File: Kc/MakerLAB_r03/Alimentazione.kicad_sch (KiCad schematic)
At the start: 25 parts, among them J4 Barrel_Jack_MountingPin, J5 Conn_01x03, J6 Conn_01x03, J7 Conn_01x03, J8 Conn_01x03, SW1 SwGenerale, U1 LM317_TO-220, U2 LM7805_TO220

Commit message: 20230309-Update
Lavoro in tandem con Marco
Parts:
- removed C3: C_Polarized, symbol Device:C_Polarized
- removed J5: Conn_01x03, Connector_PinHeader_2.54mm:PinHeader_1x03_P2.54mm_Vertical, symbol Connector_Generic:Conn_01x03
- added C16, C23, C24, C3: 100nF, Capacitor_THT:C_Disc_D7.0mm_W2.5mm_P5.00mm, symbol Device:C
- added C25: 220uF, Capacitor_THT:CP_Radial_D10.0mm_P5.00mm, symbol Device:C_Polarized
- added D20: 1N400x, symbol Device:D
- added D21, D22: LED, symbol Device:LED
- added J28, J31, J32: Conn_01x03, Connector_PinHeader_2.54mm:PinHeader_1x03_P2.54mm_Vertical, symbol Connector_Generic:Conn_01x03
- added J29, J30, J5: Conn_01x02_Male, Connector_PinSocket_2.54mm:PinSocket_1x02_P2.54mm_Vertical, symbol Connector:Conn_01x02_Male
- added Q5: 2N3904, Package_TO_SOT_THT:TO-92_Inline, symbol Transistor_BJT:2N3904
- added R22, R23, R24: R, symbol Device:R
- added TP14: VarA+, TestPoint:TestPoint_Loop_D3.80mm_Drill2.8mm, symbol Connector:TestPoint
- added TP15: VarA-, TestPoint:TestPoint_Loop_D3.80mm_Drill2.8mm, symbol Connector:TestPoint
- added TP16: 5VA+, TestPoint:TestPoint_Loop_D3.80mm_Drill2.8mm, symbol Connector:TestPoint
- added TP17: 3.3VA+, TestPoint:TestPoint_Loop_D3.80mm_Drill2.8mm, symbol Connector:TestPoint
- added TP18: 5VA-, TestPoint:TestPoint_Loop_D3.80mm_Drill2.8mm, symbol Connector:TestPoint
- added TP19: 3.3VA-, TestPoint:TestPoint_Loop_D3.80mm_Drill2.8mm, symbol Connector:TestPoint
- added U11: L78L33_SOT89, Package_TO_SOT_SMD:SOT-223, symbol Regulator_Linear:L78L33_SOT89
- C1: footprint Capacitor_THT:CP_Axial_L37.0mm_D13.0mm_P43.00mm_Horizontal -> Capacitor_THT:CP_Radial_D17.0mm_P7.50mm
- C2, C5: footprint Capacitor_THT:C_Axial_L5.1mm_D3.1mm_P7.50mm_Horizontal -> Capacitor_THT:C_Disc_D7.0mm_W2.5mm_P5.00mm
- C4: value C_Polarized -> 10uF; footprint (none) -> Capacitor_THT:CP_Radial_D5.0mm_P2.00mm
- C6: value 10uF -> 220uF; footprint Capacitor_THT:CP_Axial_L37.0mm_D13.0mm_P43.00mm_Horizontal -> Capacitor_THT:CP_Radial_D10.0mm_P5.00mm
- C7: value C_Polarized -> 220uF; footprint (none) -> Capacitor_THT:CP_Radial_D10.0mm_P5.00mm
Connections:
- net +5V: now also D21.2 (A), D22.2 (A), J29.2 (Pin_2), J30.2 (Pin_2), J31.1 (Pin_1), J31.2 (Pin_2), J31.3 (Pin_3), TP18.1, TP19.1; no longer C5.1, C6.1, D4.2 (A), U2.3 (VO)
- net +Vvar: now also J7.1 (Pin_1), J7.2 (Pin_2), J7.3 (Pin_3), C23.1, J5.2 (Pin_2), R22.2, TP15.1; no longer C7.1, D3.2 (A), D5.1 (K), R2.1, RV1.1, U1.2 (VO)
- net GND: now also C16.2, C23.2, C24.2, C25.2, C3.2, J28.1 (Pin_1), J28.2 (Pin_2), J28.3 (Pin_3), J32.1 (Pin_1), J32.2 (Pin_2), J32.3 (Pin_3), Q5.1 (E), R23.2, R24.2, U11.2 (GND); no longer J7.1 (Pin_1), J7.2 (Pin_2), J7.3 (Pin_3), R1.2
- net at C1.1, C2.1, D2.2 (A)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: now also C3.1
- new net: C7.1, D3.2 (A), D5.1 (K), J5.1 (Pin_1), R2.1, RV1.1, TP14.1, U1.2 (VO)
- new net: D21.1 (K), R23.1
- new net: C16.1, C5.1, C6.1, D20.1 (K), D4.2 (A), J29.1 (Pin_1), TP16.1, U11.3 (IN), U2.3 (VO)
- new net: C24.1, C25.1, D20.2 (A), J30.1 (Pin_1), TP17.1, U11.1 (OUT)
- new net: Q5.3 (C), R1.2
- new net: Q5.2 (B), R22.1
- new net: D22.1 (K), R24.1
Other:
- moved on the sheet: C1, D1, J4, L1, SW1

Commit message: Power Unit
Iniziato a sistemare l'unità alimentatore
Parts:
- D2: value LED -> VarOut; footprint (none) -> LED_THT:LED_D5.0mm
- D21: value LED -> +5V; footprint (none) -> LED_THT:LED_D5.0mm
- D22: value LED -> +3.3V; footprint (none) -> LED_THT:LED_D5.0mm
- R1, R2, R22, R23, R24: footprint (none) -> Resistor_THT:R_Axial_DIN0207_L6.3mm_D2.5mm_P10.16mm_Horizontal
- SW1: footprint Connector_PinSocket_2.54mm:PinSocket_1x03_P2.54mm_Vertical -> Button_Switch_THT:SW_100SP1T2B4M7QE
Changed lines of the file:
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@@
       (effects (font (size 1.27 1.27)) (justify left))
     )
-    (property "Footprint" "" (id 2) (at 220.472 50.8 90)
+    (property "Footprint" "Resistor_THT:R_Axial_DIN0207_L6.3mm_D2.5mm_P10.16mm_Horizontal" (id 2) (at 220.472 50.8 90)
       (effects (font (size 1.27 1.27)) hide)
     )
@@
       (effects (font (size 1.27 1.27)) (justify left))
     )
-    (property "Footprint" "" (id 2) (at 33.782 157.48 90)
+    (property "Footprint" "Resistor_THT:R_Axial_DIN0207_L6.3mm_D2.5mm_P10.16mm_Horizontal" (id 2) (at 33.782 157.48 90)
       (effects (font (size 1.27 1.27)) hide)
     )
@@
       (effects (font (size 1.27 1.27)) (justify left))
     )
-    (property "Footprint" "Connector_PinSocket_2.54mm:PinSocket_1x03_P2.54mm_Vertical" (id 2) (at 55.88 90.17 0)
+    (property "Footprint" "Button_Switch_THT:SW_100SP1T2B4M7QE" (id 2) (at 55.88 90.17 0)
       (effects (font (size 1.27 1.27)) hide)
     )
@@
       (effects (font (size 1.27 1.27)) (justify right))
     )
-    (property "Value" "LED" (id 1) (at 227.33 106.9974 90)
-      (effects (font (size 1.27 1.27)) (justify right))
-    )
-    (property "Footprint" "" (id 2) (at 223.52 104.14 0)
+    (property "Value" "+3.3V" (id 1) (at 227.33 106.9974 90)
+      (effects (font (size 1.27 1.27)) (justify right))
+    )
+    (property "Footprint" "LED_THT:LED_D5.0mm" (id 2) (at 223.52 104.14 0)
       (effects (font (size 1.27 1.27)) hide)
     )
@@
       (effects (font (size 1.27 1.27)) (justify left))
     )
-    (property "Footprint" "" (id 2) (at 76.962 158.75 90)
+    (property "Footprint" "Resistor_THT:R_Axial_DIN0207_L6.3mm_D2.5mm_P10.16mm_Horizontal" (id 2) (at 76.962 158.75 90)
       (effects (font (size 1.27 1.27)) hide)
     )
@@
       (effects (font (size 1.27 1.27)) (justify right))
     )
-    (property "Value" "LED" (id 1) (at 226.06 46.0374 90)
-      (effects (font (size 1.27 1.27)) (justify right))
-    )
-    (property "Footprint" "" (id 2) (at 222.25 43.18 0)
+    (property "Value" "+5V" (id 1) (at 226.06 46.0374 90)
+      (effects (font (size 1.27 1.27)) (justify right))
+    )
+    (property "Footprint" "LED_THT:LED_D5.0mm" (id 2) (at 222.25 43.18 0)
       (effects (font (size 1.27 1.27)) hide)
     )
@@
       (effects (font (size 1.27 1.27)) (justify right))
     )
-    (property "Value" "LED" (id 1) (at 39.37 152.7174 90)
-      (effects (font (size 1.27 1.27)) (justify right))
-    )
-    (property "Footprint" "" (id 2) (at 35.56 149.86 0)
+    (property "Value" "VarOut" (id 1) (at 39.37 152.7174 90)
+      (effects (font (size 1.27 1.27)) (justify right))
+    )
+    (property "Footprint" "LED_THT:LED_D5.0mm" (id 2) (at 35.56 149.86 0)
       (effects (font (size 1.27 1.27)) hide)
     )
@@
       (effects (font (size 1.27 1.27)) (justify left))
     )
-    (property "Footprint" "" (id 2) (at 221.742 111.76 90)
+    (property "Footprint" "Resistor_THT:R_Axial_DIN0207_L6.3mm_D2.5mm_P10.16mm_Horizontal" (id 2) (at 221.742 111.76 90)
       (effects (font (size 1.27 1.27)) hide)
     )
@@
       (effects (font (size 1.27 1.27)) (justify left))
     )
-    (property "Footprint" "" (id 2) (at 117.602 142.24 90)
-      (effects (font (size 1.27 1.27)) hide)
-    )
+    (property "Footprint" "Resistor_THT:R_Axial_DIN0207_L6.3mm_D2.5mm_P10.16mm_Horizontal" (id 2) (at 117.602 142.24 90)
+      (effects (font (size 1.27 1.27)) hide)
+    )

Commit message: Power Supply
Seconda fase
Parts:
- removed RV1: R_Potentiometer, symbol Device:R_Potentiometer
- added HS1, HS2: Heatsink, Heatsink2:Heatsink_28x25_Horiz, symbol Mechanical:Heatsink
- added Vmet1: 3,5_Digit_Voltmeter_3Wire, VoltmeterModule:3,5 Digit 0,28'' Voltmeter, symbol DigitalInstruments:3,5_Digit_Voltmeter_3Wire
- D1: value Ponte 1,5A -> D_Bridge_+AA-; footprint Diode_THT:Diode_Bridge_Round_D8.9mm -> Diode_THT:Diode_Bridge_Vishay_KBL; symbol Device:D_Bridge_+-AA -> Device:D_Bridge_+AA-
- D20, D4: footprint (none) -> Diode_THT:D_A-405_P10.16mm_Horizontal
- D3, D5: value D -> 1n4001; footprint (none) -> Diode_THT:D_A-405_P10.16mm_Horizontal
- Q5: value 2N3904 -> BC237; symbol Transistor_BJT:2N3904 -> Transistor_BJT:BC237
- R1: value R -> 3,3k
- R2: value R -> 240
- R22: value R -> 330k
- RV2: value R_Potentiometer -> 5K; footprint (none) -> Potentiometer_THT:Potentiometer_Omeg_PC16BU_Vertical
- U1, U2: footprint Package_TO_SOT_THT:TO-220-3_Vertical -> Package_TO_SOT_THT:TO-220-3_Horizontal_TabDown
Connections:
- net +Vvar: now also Vmet1.2 (Vin)
- net GND: now also D1.4 (-), Q5.3 (E), Vmet1.1 (GND); no longer D1.2 (-), Q5.1 (E)
- net at J4.1: now also D1.2; no longer D1.3
- net at J4.2: now also SW1.2 (B); no longer SW1.3 (C)
- net at C16.1, C5.1, C6.1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: now also Vmet1.3 (V+)
- net at R1.2: now also Q5.1 (C); no longer Q5.3 (C)
- new net: D1.3, SW1.3 (C)
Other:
- moved on the sheet: C7, D5, RV2, SW1

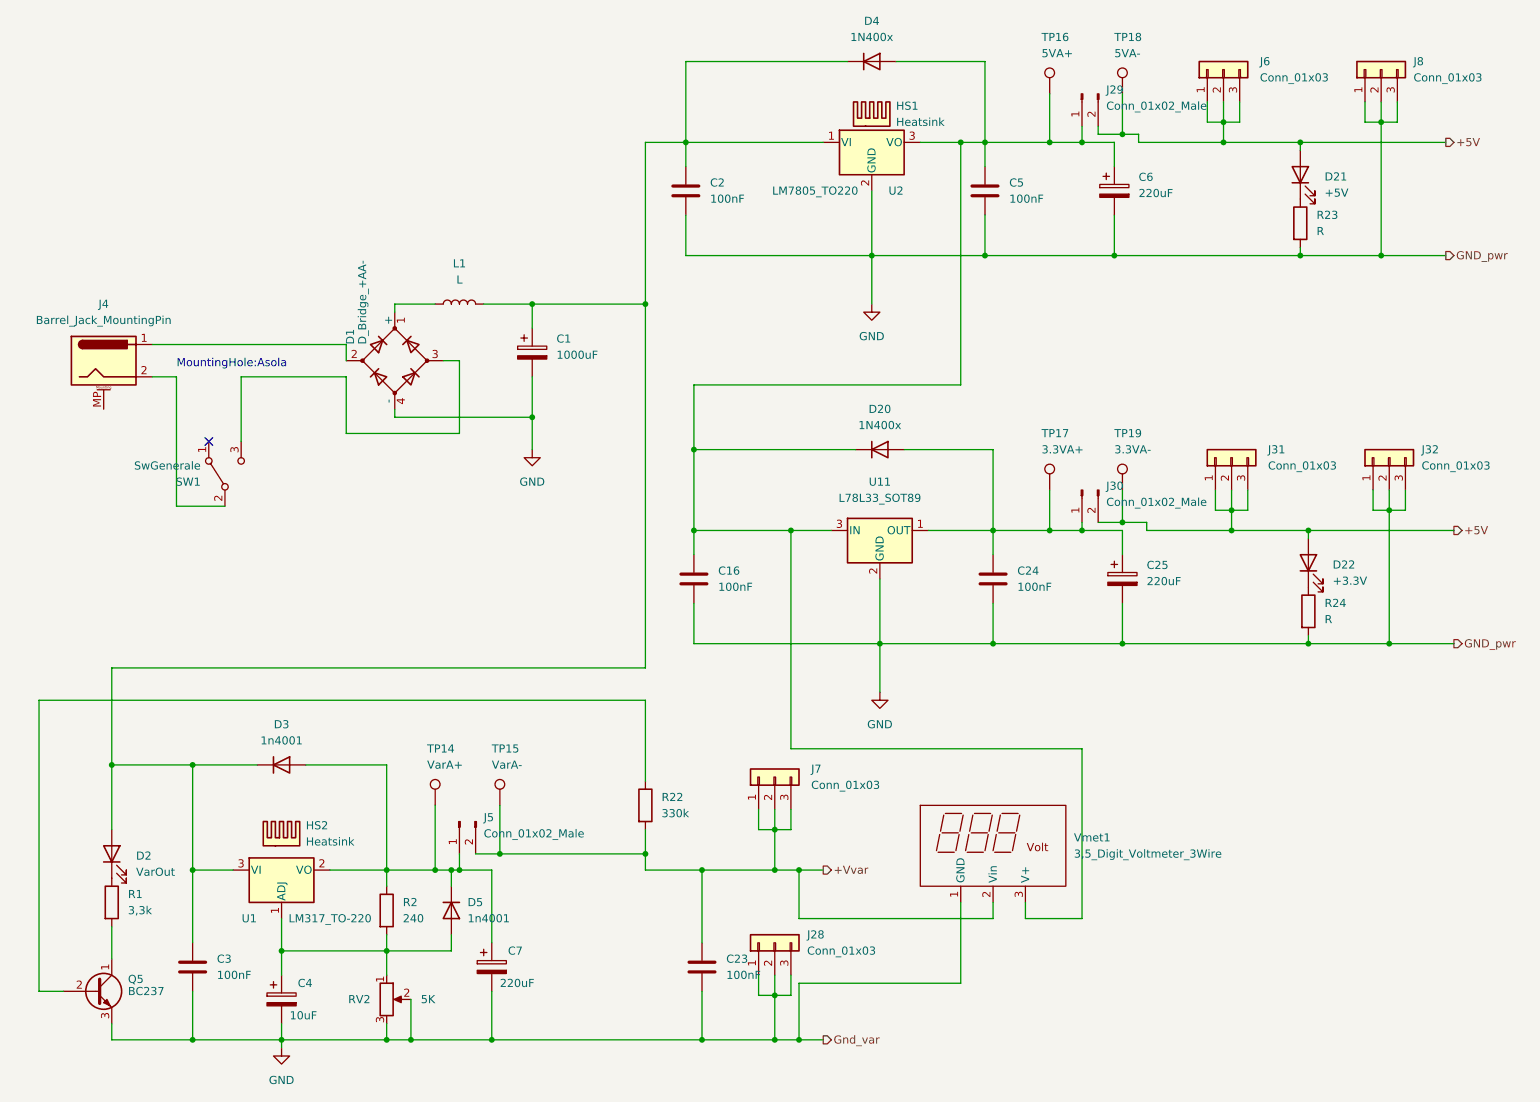
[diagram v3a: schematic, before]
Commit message: Layout Alimentatori OK
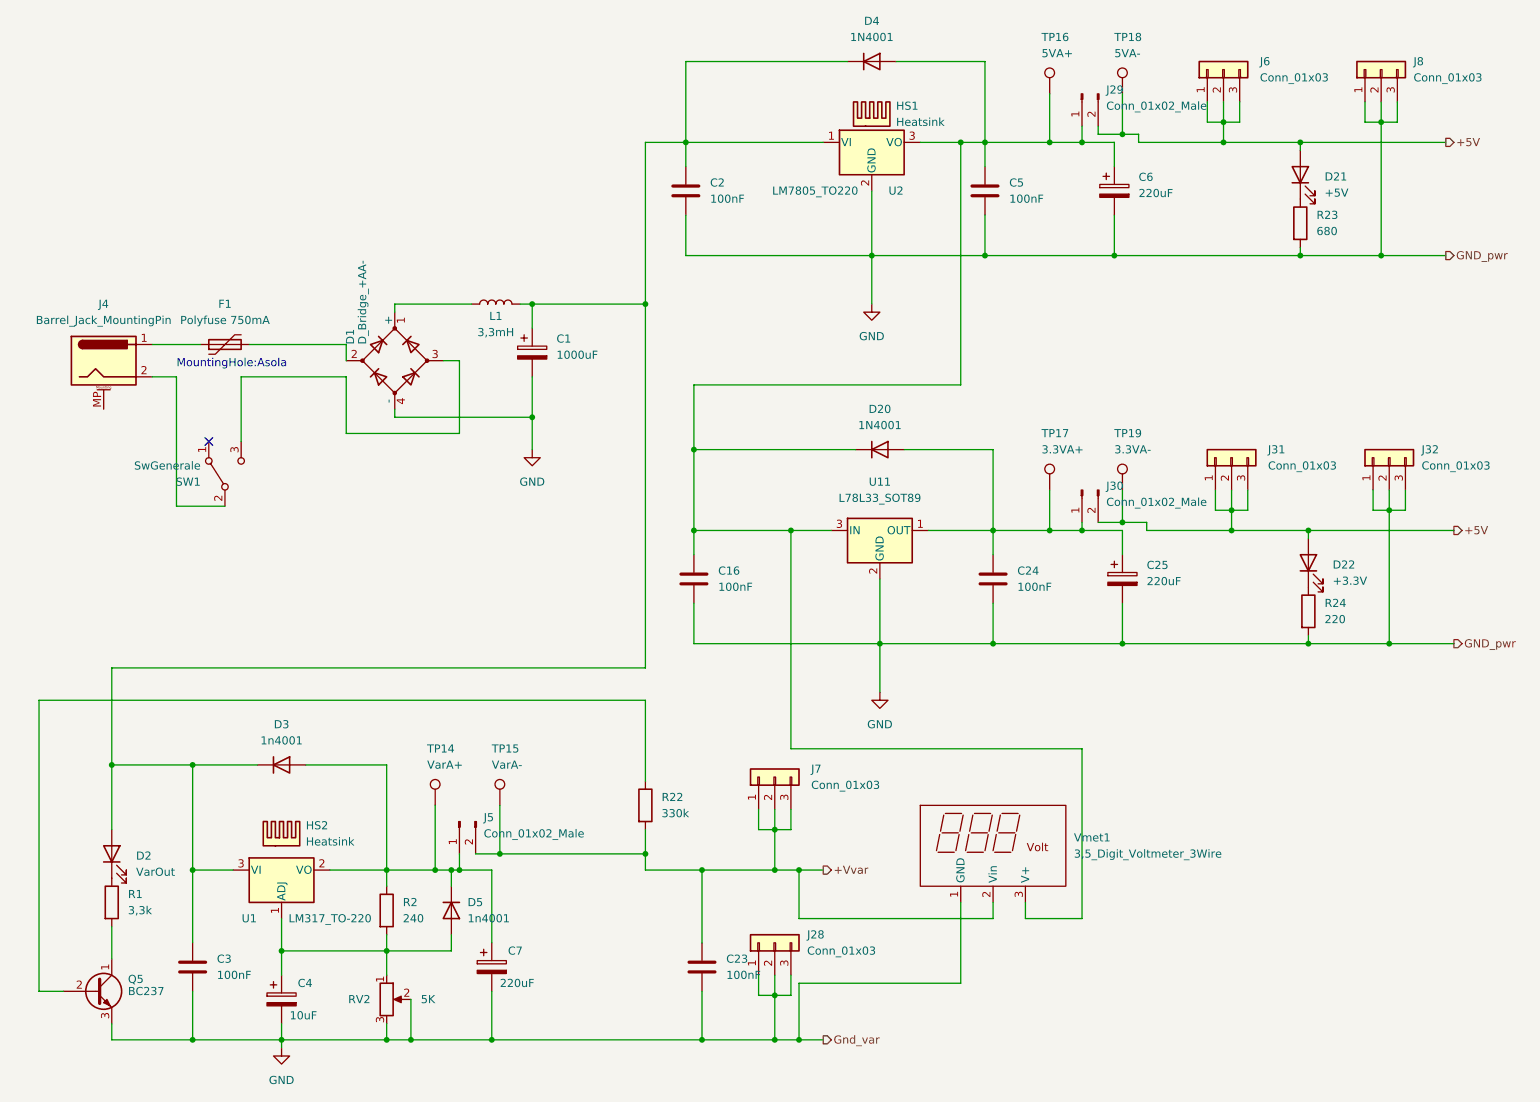
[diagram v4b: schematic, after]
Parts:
- added F1: Polyfuse 750mA, Varistor:RV_Disc_D7mm_W5.4mm_P5mm, symbol Device:Polyfuse
- D20, D4: value 1N400x -> 1N4001
- L1: value L -> 3,3mH
- R23: value R -> 680
- R24: value R -> 220
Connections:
- net at J4.1: now also F1.1; no longer D1.2
- new net: D1.2, F1.2
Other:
- moved on the sheet: L1
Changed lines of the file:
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@@
     (stroke (width 0) (type default) (color 0 0 0 0))
   )
-  (wire (pts (xy 93.98 63.5) (xy 101.6 63.5))
+  (wire (pts (xy 99.695 63.5) (xy 101.6 63.5))
     (stroke (width 0) (type default) (color 0 0 0 0))
   )
@@
     (stroke (width 0) (type default) (color 0 0 0 0))
   )
+  (wire (pts (xy 57.15 69.85) (xy 72.39 69.85))
+    (stroke (width 0) (type default) (color 0 0 0 0))
+  )
   (wire (pts (xy 92.71 149.86) (xy 96.52 149.86))
     (stroke (width 0) (type default) (color 0 0 0 0))
@@
     (stroke (width 0) (type default) (color 0 0 0 0))
   )
-  (wire (pts (xy 86.36 63.5) (xy 80.01 63.5))
+  (wire (pts (xy 80.01 63.5) (xy 92.075 63.5))
     (stroke (width 0) (type default) (color 0 0 0 0))
   )
@@
     (stroke (width 0) (type default) (color 0 0 0 0))
   )
-  (wire (pts (xy 41.91 69.85) (xy 72.39 69.85))
+  (wire (pts (xy 41.91 69.85) (xy 49.53 69.85))
     (stroke (width 0) (type default) (color 0 0 0 0))
   )
@@
       (effects (font (size 1.27 1.27)) (justify left))
     )
-    (property "Value" "R" (id 1) (at 224.79 52.0699 0)
+    (property "Value" "680" (id 1) (at 224.79 52.0699 0)
       (effects (font (size 1.27 1.27)) (justify left))
     )
@@
     )
     (property "Datasheet" "~" (id 3) (at 222.25 50.8 0)
+      (effects (font (size 1.27 1.27)) hide)
+    )
+    (pin "1")
+    (pin "2")
+  )
+  (symbol (lib_id "Device:Polyfuse") (at 53.34 69.85 90) (unit 1)
+    (in_bom yes) (on_board yes) (fields_autoplaced)
+    (property "Reference" "F1" (id 0) (at 53.34 63.5 90))
+    (property "Value" "Polyfuse 750mA" (id 1) (at 53.34 66.04 90))
+    (property "Footprint" "Varistor:RV_Disc_D7mm_W5.4mm_P5mm" (id 2) (at 58.42 68.58 0)
+      (effects (font (size 1.27 1.27)) (justify left) hide)
+    )
+    (property "Datasheet" "~" (id 3) (at 53.34 69.85 0)
       (effects (font (size 1.27 1.27)) hide)
     )
@@
     (in_bom yes) (on_board yes) (fields_autoplaced)
     (property "Reference" "D20" (id 0) (at 156.21 80.01 0))
-    (property "Value" "1N400x" (id 1) (at 156.21 82.55 0))
+    (property "Value" "1N4001" (id 1) (at 156.21 82.55 0))
     (property "Footprint" "Diode_THT:D_A-405_P10.16mm_Horizontal" (id 2) (at 156.21 86.36 0)
       (effects (font (size 1.27 1.27)) hide)
@@
     (pin "2")
   )
-  (symbol (lib_id "Device:L") (at 90.17 63.5 90) (unit 1)
-    (in_bom yes) (on_board yes) (fields_autoplaced)
-    (property "Reference" "L1" (id 0) (at 90.17 57.15 90))
-    (property "Value" "L" (id 1) (at 90.17 59.69 90))
-    (property "Footprint" "Inductor_THT:L_Axial_L12.0mm_D5.0mm_P15.24mm_Horizontal_Fastron_MISC" (id 2) (at 90.17 63.5 0)
-      (effects (font (size 1.27 1.27)) hide)
-    )
-    (property "Datasheet" "~" (id 3) (at 90.17 63.5 0)
+  (symbol (lib_id "Device:L") (at 95.885 63.5 90) (unit 1)
+    (in_bom yes) (on_board yes)
+    (property "Reference" "L1" (id 0) (at 95.885 65.405 90))
+    (property "Value" "3,3mH" (id 1) (at 95.885 67.945 90))
+    (property "Footprint" "Inductor_THT:L_Axial_L12.0mm_D5.0mm_P15.24mm_Horizontal_Fastron_MISC" (id 2) (at 95.885 63.5 0)
+      (effects (font (size 1.27 1.27)) hide)
+    )
+    (property "Datasheet" "~" (id 3) (at 95.885 63.5 0)
       (effects (font (size 1.27 1.27)) hide)
     )
@@
       (effects (font (size 1.27 1.27)) (justify left))
     )
-    (property "Value" "R" (id 1) (at 226.06 113.0299 0)
+    (property "Value" "220" (id 1) (at 226.06 113.0299 0)
       (effects (font (size 1.27 1.27)) (justify left))
     )
@@
     (in_bom yes) (on_board yes) (fields_autoplaced)
     (property "Reference" "D4" (id 0) (at 154.94 19.05 0))
-    (property "Value" "1N400x" (id 1) (at 154.94 21.59 0))
+    (property "Value" "1N4001" (id 1) (at 154.94 21.59 0))
     (property "Footprint" "Diode_THT:D_A-405_P10.16mm_Horizontal" (id 2) (at 154.94 25.4 0)
       (effects (font (size 1.27 1.27)) hide)
